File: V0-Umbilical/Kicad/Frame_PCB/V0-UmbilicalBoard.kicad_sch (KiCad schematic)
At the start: 16 parts, among them J1 Conn_02x08_Odd_Even, J10 Neopixel Strip 1, J11 Neopixel Strip 1, J12 Neopixel Out, J2 Motor, J3 Hotend Fan, J4 Part Cooling Fan, J5 Heater, J6 Thermistor, J7 X-Endstop, J8 Chamber Thermistor, J9 Neopixel (from controller)

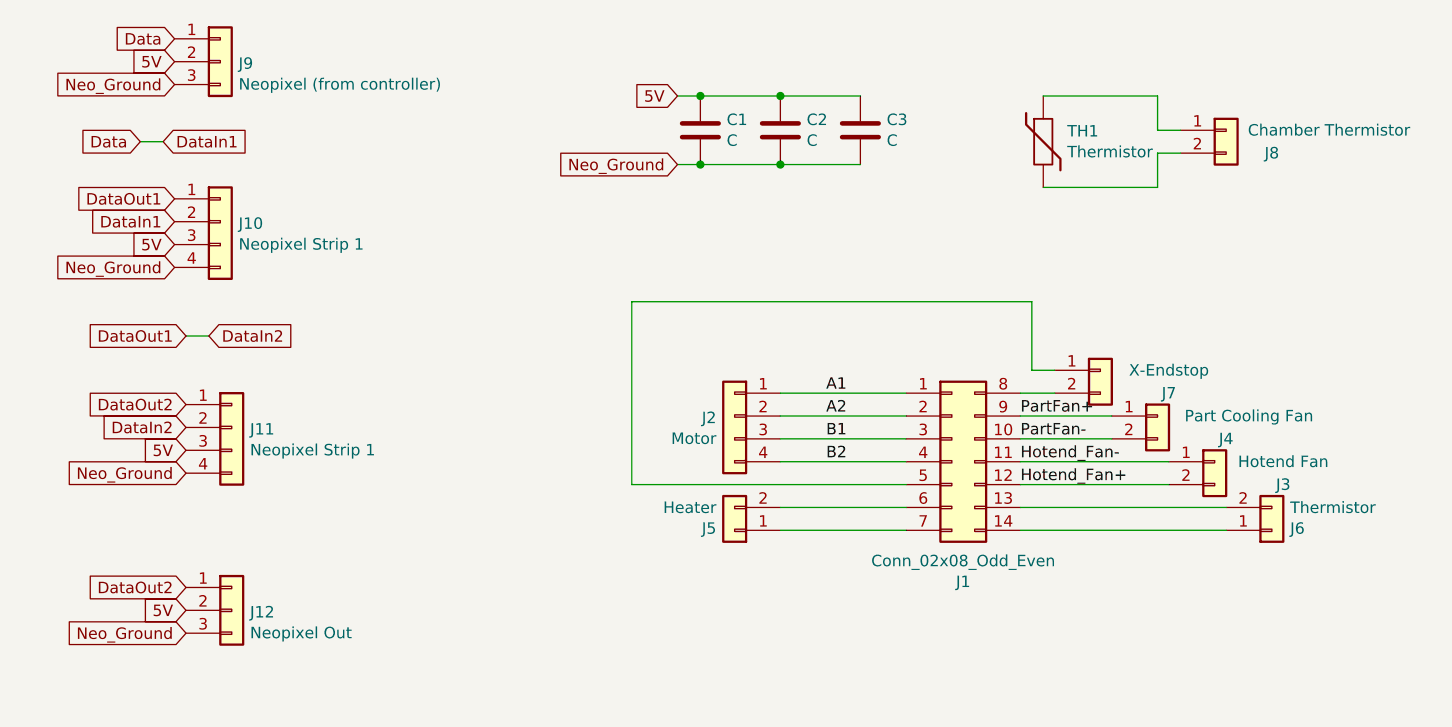
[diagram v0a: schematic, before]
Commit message: Fix KiCad 6 model errors and add images (#174)
Fix Kicad 6 model linking errors and update images with Rev A.1 traces.
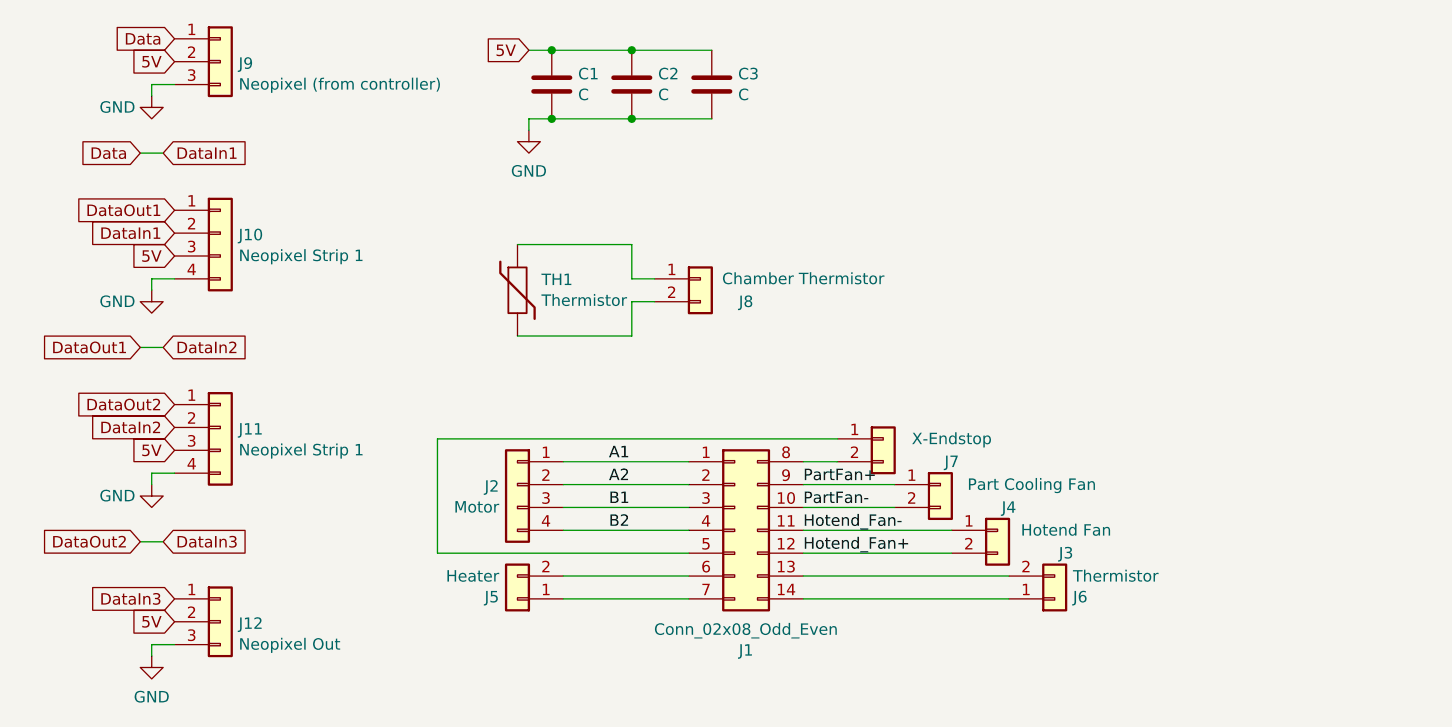
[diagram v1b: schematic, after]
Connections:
- net DataOut2 renamed DataIn3
- net Neo_Ground renamed GND
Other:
- moved on the sheet: C1, C2, C3, J1, J10, J11, J12, J2, J3, J4, J5, J6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
